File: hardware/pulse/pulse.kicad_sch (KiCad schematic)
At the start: 44 parts, among them J101 Cortex, SW101 SKSG, SW102 SKSG, U101 TPS78433QWDRBRQ1, U102 ATSAMD51J, Y101 32k768

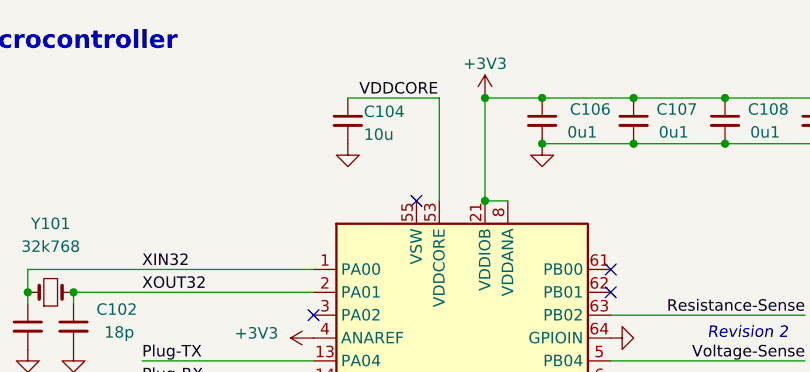
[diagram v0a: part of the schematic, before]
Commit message: Switch to 6 layer
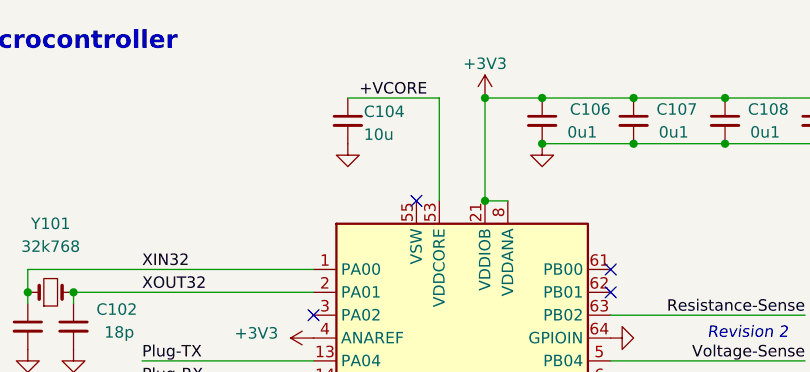
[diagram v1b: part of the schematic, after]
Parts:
- D102: footprint V2_LED:LED_0603 -> V2_LED:LED_1608
- INFO101: value Layer_Numbers -> Layer_Numbers-6; footprint V2_Production:Layer_Numbers -> V2_Production:Layer_Numbers-6; symbol V2_Production:Layer_Numbers -> V2_Production:Layer_Numbers-6
- TVS101: footprint V2_Diode_SMD:D_0603 -> V2_Diode_SMD:D_1608
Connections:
- net VDDCORE renamed +VCORE
